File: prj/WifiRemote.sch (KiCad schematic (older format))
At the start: 68 parts, among them J1 DIP-BLACK-MALE-HEADER-VERT_4P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, J2 DIP-BLACK-MALE-HEADER_6P-2.54_, K1 DIP-SWITCH-TACTILE-SPST-NO_TS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, K2 DIP-SWITCH-TACTILE-SPST-NO_TS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, K3 DIP-SWITCH-TACTILE-SPST-NO_TS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, K4 DIP-SWITCH-TACTILE-SPST-NO_TS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, M1 Mechanical_Mount, M2 Mechanical_Mount, M3 Mechanical_Mount, M4 Mechanical_Mount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

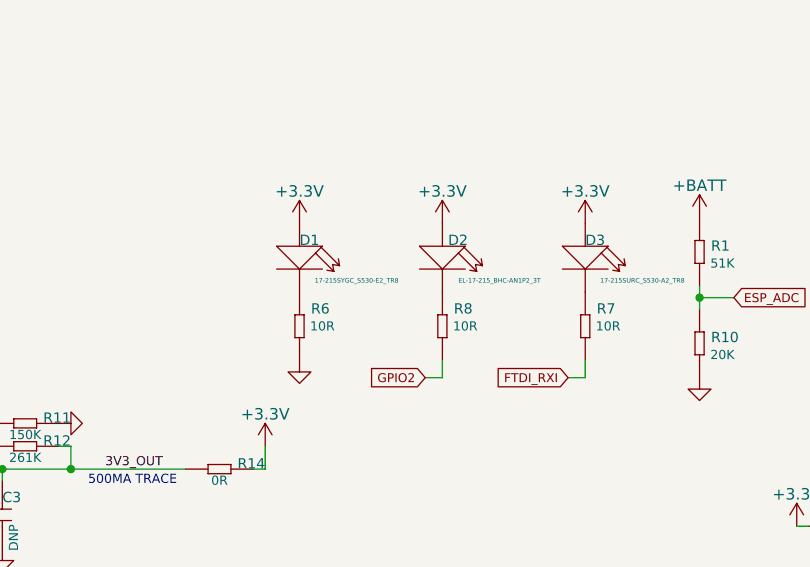
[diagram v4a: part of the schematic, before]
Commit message: Swapped D1 and D2 for layout
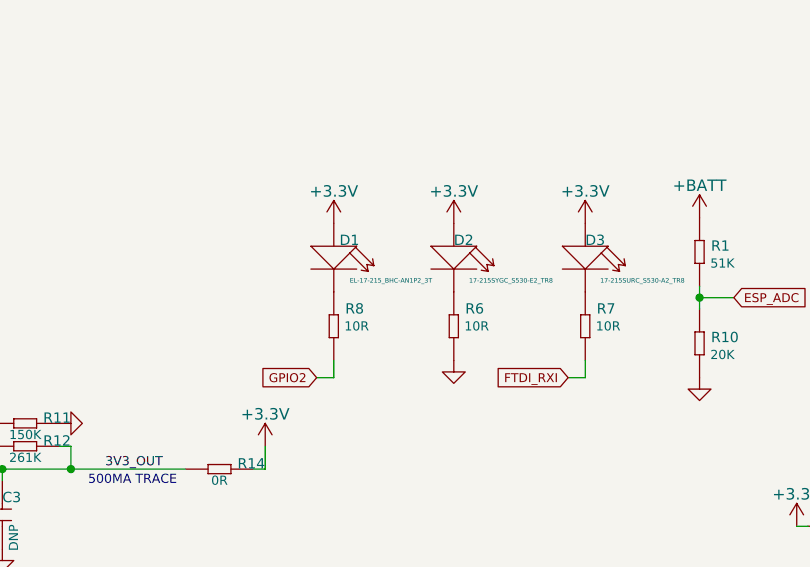
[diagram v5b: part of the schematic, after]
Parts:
- renumbered D2 to D1, D1 to D2
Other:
- moved on the sheet: D1, D2, R6, R8
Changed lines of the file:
@@
 $EndComp
 $Comp
-L SMD-LED-CLEAR-GREEN_0805_ D1
+L SMD-LED-CLEAR-GREEN_0805_ D2
 U 1 1 59B8B400
-P 4800 1225
-F 0 "D1" V 4750 1225 45  0000 L BNN
-F 1 "SMD-LED-CLEAR-GREEN_0805_" H 4600 1025 45  0001 L BNN
-F 2 "SeeedOPL-LED-2016:LED-0805" H 4800 1225 60  0001 C CNN
-F 3 "" H 4800 1225 60  0000 C CNN
-F 4 "17-215SYGC_S530-E2_TR8" V 4900 1475 20  0000 C CNN "MPN"
-F 5 "304090057" H 4830 1375 20  0001 C CNN "SKU"
-	1    4800 1225
+P 5475 1225
+F 0 "D2" V 5425 1225 45  0000 L BNN
+F 1 "SMD-LED-CLEAR-GREEN_0805_" H 5275 1025 45  0001 L BNN
+F 2 "SeeedOPL-LED-2016:LED-0805" H 5475 1225 60  0001 C CNN
+F 3 "" H 5475 1225 60  0000 C CNN
+F 4 "17-215SYGC_S530-E2_TR8" V 5575 1475 20  0000 C CNN "MPN"
+F 5 "304090057" H 5505 1375 20  0001 C CNN "SKU"
+	1    5475 1225
 	0    1    1    0
 $EndComp
@@
 L +3.3V #PWR024
 U 1 1 59B8BA53
-P 4800 1075
-F 0 "#PWR024" H 4800 925 50  0001 C CNN
-F 1 "+3.3V" H 4800 1215 50  0000 C CNN
-F 2 "" H 4800 1075 50  0000 C CNN
-F 3 "" H 4800 1075 50  0000 C CNN
-	1    4800 1075
+P 5475 1075
+F 0 "#PWR024" H 5475 925 50  0001 C CNN
+F 1 "+3.3V" H 5475 1215 50  0000 C CNN
+F 2 "" H 5475 1075 50  0000 C CNN
+F 3 "" H 5475 1075 50  0000 C CNN
+	1    5475 1075
 	1    0    0    -1
 $EndComp
@@
 L SMD-RES-10R-5%-1_10W_0603_ R6
 U 1 1 59B8BFB0
-P 4800 1525
-F 0 "R6" V 4750 1575 45  0000 L BNN
-F 1 "SMD-RES-10R-5%-1_10W_0603_" H 4650 1425 45  0001 L BNN
-F 2 "SeeedOPL-Resistor-2016:R0603" H 4800 1525 40  0001 C CNN
-F 3 "" H 4800 1525 40  0001 C CNN
-F 4 "RC0603JR-0710RL" H 4830 1675 20  0001 C CNN "MPN"
-F 5 "301010096" H 4830 1675 20  0001 C CNN "SKU"
-F 6 "10R" V 4800 1625 40  0000 C CNN "RESISTANCE"
-	1    4800 1525
+P 5475 1525
+F 0 "R6" V 5425 1575 45  0000 L BNN
+F 1 "SMD-RES-10R-5%-1_10W_0603_" H 5325 1425 45  0001 L BNN
+F 2 "SeeedOPL-Resistor-2016:R0603" H 5475 1525 40  0001 C CNN
+F 3 "" H 5475 1525 40  0001 C CNN
+F 4 "RC0603JR-0710RL" H 5505 1675 20  0001 C CNN "MPN"
+F 5 "301010096" H 5505 1675 20  0001 C CNN "SKU"
+F 6 "10R" V 5475 1625 40  0000 C CNN "RESISTANCE"
+	1    5475 1525
 	0    1    1    0
 $EndComp
@@
 L GNDD #PWR025
 U 1 1 59B8C077
-P 4800 1675
-F 0 "#PWR025" H 4800 1425 50  0001 C CNN
-F 1 "GNDD" H 4800 1525 50  0001 C CNN
-F 2 "" H 4800 1675 50  0000 C CNN
-F 3 "" H 4800 1675 50  0000 C CNN
-	1    4800 1675
+P 5475 1675
+F 0 "#PWR025" H 5475 1425 50  0001 C CNN
+F 1 "GNDD" H 5475 1525 50  0001 C CNN
+F 2 "" H 5475 1675 50  0000 C CNN
+F 3 "" H 5475 1675 50  0000 C CNN
+	1    5475 1675
 	1    0    0    -1
 $EndComp
@@
 	0    -1   -1   0
 $EndComp
-Text GLabel 5350 1750 0    39   Input ~ 0
+Text GLabel 4875 1750 0    39   Input ~ 0
 GPIO2
 Text GLabel 8000 1250 0    39   Input ~ 0
@@
 L SMD-RES-10R-5%-1_10W_0603_ R8
 U 1 1 59B9052C
-P 5425 1525
-F 0 "R8" V 5375 1575 45  0000 L BNN
-F 1 "SMD-RES-10R-5%-1_10W_0603_" H 5275 1425 45  0001 L BNN
-F 2 "SeeedOPL-Resistor-2016:R0603" H 5425 1525 40  0001 C CNN
-F 3 "" H 5425 1525 40  0001 C CNN
-F 4 "RC0603JR-0710RL" H 5455 1675 20  0001 C CNN "MPN"
-F 5 "301010096" H 5455 1675 20  0001 C CNN "SKU"
-F 6 "10R" V 5425 1625 40  0000 C CNN "RESISTANCE"
-	1    5425 1525
+P 4950 1525
+F 0 "R8" V 4900 1575 45  0000 L BNN
+F 1 "SMD-RES-10R-5%-1_10W_0603_" H 4800 1425 45  0001 L BNN
+F 2 "SeeedOPL-Resistor-2016:R0603" H 4950 1525 40  0001 C CNN
+F 3 "" H 4950 1525 40  0001 C CNN
+F 4 "RC0603JR-0710RL" H 4980 1675 20  0001 C CNN "MPN"
+F 5 "301010096" H 4980 1675 20  0001 C CNN "SKU"
+F 6 "10R" V 4950 1625 40  0000 C CNN "RESISTANCE"
+	1    4950 1525
 	0    1    1    0
 $EndComp
@@
 L +3.3V #PWR030
 U 1 1 59B94182
-P 5425 1075
-F 0 "#PWR030" H 5425 925 50  0001 C CNN
-F 1 "+3.3V" H 5425 1215 50  0000 C CNN
-F 2 "" H 5425 1075 50  0000 C CNN
-F 3 "" H 5425 1075 50  0000 C CNN
-	1    5425 1075
+P 4950 1075
+F 0 "#PWR030" H 4950 925 50  0001 C CNN
+F 1 "+3.3V" H 4950 1215 50  0000 C CNN
+F 2 "" H 4950 1075 50  0000 C CNN
+F 3 "" H 4950 1075 50  0000 C CNN
+	1    4950 1075
 	1    0    0    -1
 $EndComp
@@
 	7850 2425 7850 2400
 Wire Wire Line
-	5350 1750 5425 1750
-Wire Wire Line
-	5425 1750 5425 1675
+	4875 1750 4950 1750
+Wire Wire Line
+	4950 1750 4950 1675
 Wire Wire Line
 	5975 1750 6050 1750
@@
 MOUNTING HARDWARE
 $Comp
-L SMD-LED-CLEAR-BLUE_0805_ D2
+L SMD-LED-CLEAR-BLUE_0805_ D1
 U 1 1 59C1E2BF
-P 5425 1225
-F 0 "D2" V 5375 1250 45  0000 L BNN
-F 1 "SMD-LED-CLEAR-BLUE_0805_" H 5225 1025 45  0001 L BNN
-F 2 "SeeedOPL-LED-2016:LED-0805" H 5425 1225 60  0001 C CNN
-F 3 "" H 5425 1225 60  0001 C CNN
-F 4 "EL-17-215_BHC-AN1P2_3T" V 5525 1475 20  0000 C CNN "MPN"
-F 5 "304090061" H 5455 1375 20  0001 C CNN "SKU"
-	1    5425 1225
-	0    1    1    0
-$EndComp
+P 4950 1225
+F 0 "D1" V 4900 1250 45  0000 L BNN
+F 1 "SMD-LED-CLEAR-BLUE_0805_" H 4750 1025 45  0001 L BNN
+F 2 "SeeedOPL-LED-2016:LED-0805" H 4950 1225 60  0001 C CNN
+F 3 "" H 4950 1225 60  0001 C CNN
+F 4 "EL-17-215_BHC-AN1P2_3T" V 5050 1475 20  0000 C CNN "MPN"
+F 5 "304090061" H 4980 1375 20  0001 C CNN "SKU"
+	1    4950 1225
+	0    1    1    0
+$EndComp

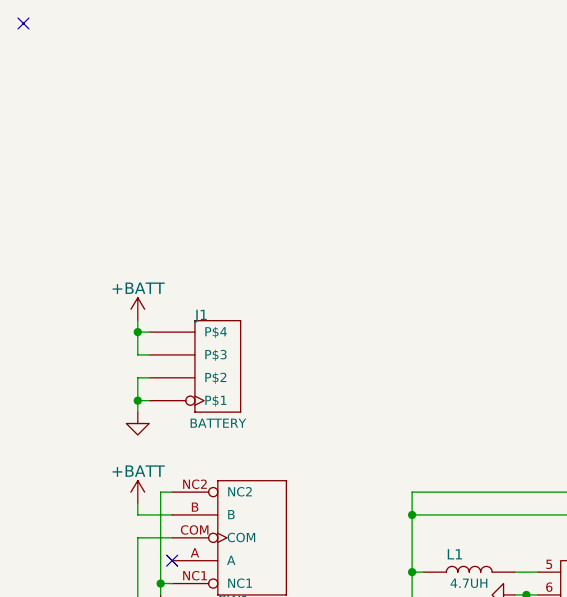
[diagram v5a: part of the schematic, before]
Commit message: Updated battery connector
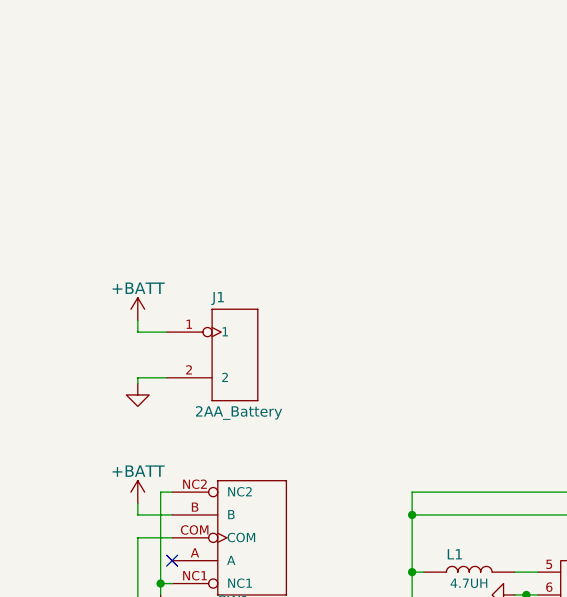
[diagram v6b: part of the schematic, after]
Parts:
- removed J1: DIP-BLACK-MALE-HEADER-VERT_4P-2.54_, SeeedOPL-Connector-2016:H4-2.54, symbol DIP-BLACK-MALE-HEADER-VERT_4P-2.54_
- added J1: 2AA_Battery, SeeedOPL-Connector-2016:H2-2.54, symbol 2AA_Battery
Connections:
- net +BATT: now also J1.1
- net GNDD: now also J1.2
- no-connect marks 11 -> 10
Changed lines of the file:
@@
 LIBS:ICEE-Diode
 LIBS:ICEE-Mechanical
+LIBS:ICEE-Battery
 EELAYER 25 0
 EELAYER END
@@
 	1    0    0    -1
 $EndComp
-NoConn ~ 250  -550
-$Comp
-L DIP-BLACK-MALE-HEADER-VERT_4P-2.54_ J1
-U 1 1 59B7E14C
-P 1100 950
-F 0 "J1" H 1000 700 45  0000 L BNN
-F 1 "DIP-BLACK-MALE-HEADER-VERT_4P-2.54_" H 1050 1200 45  0001 L BNN
-F 2 "SeeedOPL-Connector-2016:H4-2.54" H 1100 950 60  0001 C CNN
-F 3 "" H 1100 950 60  0001 C CNN
-F 4 "P125-1104A0BS116A1" H 1130 1100 20  0001 C CNN "MPN"
-F 5 "320020017" H 1130 1100 20  0001 C CNN "SKU"
-F 6 "BATTERY" H 1100 1200 40  0000 C CNN "DESCRIPTION"
-	1    1100 950
-	1    0    0    1
-$EndComp
 $Comp
 L GNDD #PWR023
 U 1 1 59B82986
-P 750 1150
-F 0 "#PWR023" H 750 900 50  0001 C CNN
-F 1 "GNDD" H 750 1000 50  0001 C CNN
-F 2 "" H 750 1150 50  0000 C CNN
-F 3 "" H 750 1150 50  0000 C CNN
-	1    750  1150
+P 750 1025
+F 0 "#PWR023" H 750 775 50  0001 C CNN
+F 1 "GNDD" H 750 875 50  0001 C CNN
+F 2 "" H 750 1025 50  0000 C CNN
+F 3 "" H 750 1025 50  0000 C CNN
+	1    750  1025
 	1    0    0    -1
 $EndComp
@@
 Connection ~ 4275 5625
 Wire Wire Line
-	800  800  750  800
-Wire Wire Line
-	750  750  750  900
-Wire Wire Line
-	750  900  800  900
-Connection ~ 750  800
-Wire Wire Line
-	800  1000 750  1000
-Wire Wire Line
-	750  1000 750  1150
-Wire Wire Line
-	750  1100 800  1100
-Connection ~ 750  1100
-Wire Wire Line
 	6975 2400 7025 2400
 Wire Wire Line
@@
 	1    0    0    -1
 $EndComp
+$Comp
+L 2AA_Battery J1
+U 1 1 59C7F15C
+P 1175 900
+F 0 "J1" H 1075 1125 45  0000 L BNN
+F 1 "2AA_Battery" H 1000 625 45  0000 L BNN
+F 2 "SeeedOPL-Connector-2016:H2-2.54" H 1175 900 60  0001 C CNN
+F 3 "" H 1175 900 60  0001 C CNN
+F 4 "BH-321-1A" H 1205 1050 20  0001 C CNN "MPN"
+F 5 "320180001" H 1205 1050 20  0001 C CNN "SKU"
+	1    1175 900
+	1    0    0    -1
+$EndComp
+Wire Wire Line
+	875  800  750  800
+Wire Wire Line
+	750  800  750  750
+Wire Wire Line
+	875  1000 750  1000
+Wire Wire Line
+	750  1000 750  1025
 $EndSCHEMATC

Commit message: Added footprint for header_1x2
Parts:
- J1: footprint SeeedOPL-Connector-2016:H2-2.54 -> ICEE-Connector:header_1x2
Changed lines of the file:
@@
-	1    0    0    -1
-$EndComp
-$Comp
-L 2AA_Battery J1
-U 1 1 59C7F15C
-P 1175 900
-F 0 "J1" H 1075 1125 45  0000 L BNN
-F 1 "2AA_Battery" H 1000 625 45  0000 L BNN
-F 2 "SeeedOPL-Connector-2016:H2-2.54" H 1175 900 60  0001 C CNN
-F 3 "" H 1175 900 60  0001 C CNN
-F 4 "BH-321-1A" H 1205 1050 20  0001 C CNN "MPN"
-F 5 "320180001" H 1205 1050 20  0001 C CNN "SKU"
-	1    1175 900
 	1    0    0    -1
 $EndComp
@@
 Wire Wire Line
 	750  1000 750  1025
+$Comp
+L 2AA_Battery J1
+U 1 1 59C7F5DA
+P 1175 900
+F 0 "J1" H 1075 1125 45  0000 L BNN
+F 1 "2AA_Battery" H 1000 625 45  0000 L BNN
+F 2 "ICEE-Connector:header_1x2" H 1175 900 60  0001 C CNN
+F 3 "" H 1175 900 60  0001 C CNN
+F 4 "BH-321-1A" H 1205 1050 20  0001 C CNN "MPN"
+F 5 "320180001" H 1205 1050 20  0001 C CNN "SKU"
+	1    1175 900
+	1    0    0    -1
+$EndComp
 $EndSCHEMATC

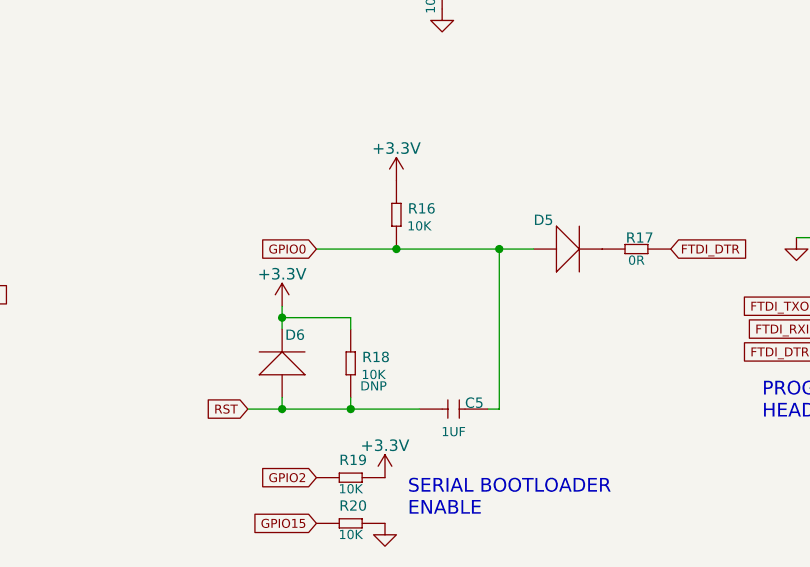
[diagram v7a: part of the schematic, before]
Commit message: Swapped diode packages
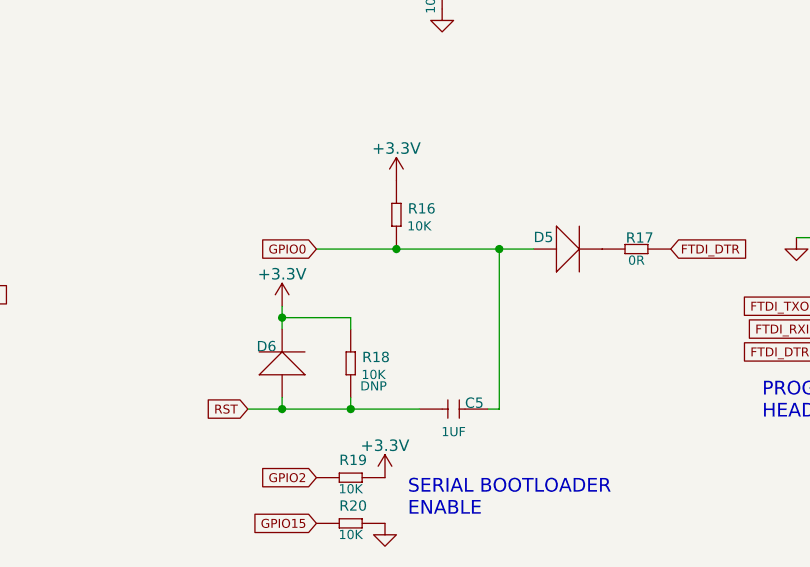
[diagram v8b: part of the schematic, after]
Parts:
- removed D11, D7, D8, D9: SMD-DIODE-SWITCH-1N4148_LL-34_, SeeedOPL-Diode-2016:LL-34, symbol SMD-DIODE-SWITCH-1N4148_LL-34_
- removed D5, D6: SMD-DIODE-SCHOTTKY-20V-500MA_SOD-123_, SeeedOPL-Diode-2016:SOD-123, symbol SMD-DIODE-SCHOTTKY-20V-500MA_SOD-123_
- added D11, D5, D6, D7, D8, D9: SMD-DIODE-SCHOTTKY-20V-1A_SOD-123_, symbol SMD-DIODE-SCHOTTKY-20V-1A_SOD-123_
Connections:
- net +3V3: now also D6.-
- net GPIO0: now also D5.+
- net GPIO13: now also D11.+, D7.+, D8.+, D9.+
- net RST: now also D6.+
- net SW1: now also D7.-
- net SW2: now also D8.-
- net SW3: now also D9.-
- net SW4: now also D11.-
- net at R17.2: now also D5.-
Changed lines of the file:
@@
 GPIO14
-$Comp
-L SMD-DIODE-SWITCH-1N4148_LL-34_ D9
-U 1 1 59AF0C4B
-P 4825 4475
-F 0 "D9" H 4675 4575 45  0000 L BNN
-F 1 "SMD-DIODE-SWITCH-1N4148_LL-34_" H 4675 4325 45  0001 L BNN
-F 2 "SeeedOPL-Diode-2016:LL-34" H 4825 4475 60  0001 C CNN
-F 3 "" H 4825 4475 60  0001 C CNN
-F 4 "1N4148" H 4855 4625 20  0001 C CNN "MPN"
-F 5 "304040016" H 4855 4625 20  0001 C CNN "SKU"
-	1    4825 4475
-	-1   0    0    1
-$EndComp
-$Comp
-L SMD-DIODE-SWITCH-1N4148_LL-34_ D11
-U 1 1 59AF1CC4
-P 4825 4725
-F 0 "D11" H 4675 4825 45  0000 L BNN
-F 1 "SMD-DIODE-SWITCH-1N4148_LL-34_" H 4675 4575 45  0001 L BNN
-F 2 "SeeedOPL-Diode-2016:LL-34" H 4825 4725 60  0001 C CNN
-F 3 "" H 4825 4725 60  0001 C CNN
-F 4 "1N4148" H 4855 4875 20  0001 C CNN "MPN"
-F 5 "304040016" H 4855 4875 20  0001 C CNN "SKU"
-	1    4825 4725
-	-1   0    0    1
-$EndComp
-$Comp
-L SMD-DIODE-SWITCH-1N4148_LL-34_ D8
-U 1 1 59AF1E3D
-P 4825 4225
-F 0 "D8" H 4675 4325 45  0000 L BNN
-F 1 "SMD-DIODE-SWITCH-1N4148_LL-34_" H 4675 4075 45  0001 L BNN
-F 2 "SeeedOPL-Diode-2016:LL-34" H 4825 4225 60  0001 C CNN
-F 3 "" H 4825 4225 60  0001 C CNN
-F 4 "1N4148" H 4855 4375 20  0001 C CNN "MPN"
-F 5 "304040016" H 4855 4375 20  0001 C CNN "SKU"
-	1    4825 4225
-	-1   0    0    1
-$EndComp
-$Comp
-L SMD-DIODE-SWITCH-1N4148_LL-34_ D7
-U 1 1 59AF1EFF
-P 4825 3975
-F 0 "D7" H 4675 4075 45  0000 L BNN
-F 1 "SMD-DIODE-SWITCH-1N4148_LL-34_" H 4675 3825 45  0001 L BNN
-F 2 "SeeedOPL-Diode-2016:LL-34" H 4825 3975 60  0001 C CNN
-F 3 "" H 4825 3975 60  0001 C CNN
-F 4 "1N4148" H 4855 4125 20  0001 C CNN "MPN"
-F 5 "304040016" H 4855 4125 20  0001 C CNN "SKU"
-	1    4825 3975
-	-1   0    0    1
-$EndComp
 $Comp
 L SMD-RES-10K-5%-1_10W_0603_ R26
@@
 	1    5225 3775
 	0    1    1    0
-$EndComp
-$Comp
-L SMD-DIODE-SCHOTTKY-20V-500MA_SOD-123_ D5
-U 1 1 59AFC988
-P 8400 3775
-F 0 "D5" H 8250 3875 45  0000 L BNN
-F 1 "SMD-DIODE-SCHOTTKY-20V-500MA_SOD-123_" H 8250 3625 45  0001 L BNN
-F 2 "SeeedOPL-Diode-2016:SOD-123" H 8400 3775 60  0001 C CNN
-F 3 "" H 8400 3775 60  0001 C CNN
-F 4 "SS0520-7-F" H 8430 3925 20  0001 C CNN "MPN"
-F 5 "304020032" H 8430 3925 20  0001 C CNN "SKU"
-	1    8400 3775
-	1    0    0    -1
 $EndComp
 $Comp
@@
 	1    0    0    -1
 $EndComp
-$Comp
-L SMD-DIODE-SCHOTTKY-20V-500MA_SOD-123_ D6
-U 1 1 59B9AAAC
-P 7150 4275
-F 0 "D6" V 7300 4175 45  0000 L BNN
-F 1 "SMD-DIODE-SCHOTTKY-20V-500MA_SOD-123_" H 7000 4125 45  0001 L BNN
-F 2 "SeeedOPL-Diode-2016:SOD-123" H 7150 4275 60  0001 C CNN
-F 3 "" H 7150 4275 60  0001 C CNN
-F 4 "SS0520-7-F" H 7180 4425 20  0001 C CNN "MPN"
-F 5 "304020032" H 7180 4425 20  0001 C CNN "SKU"
-	1    7150 4275
-	0    -1   -1   0
-$EndComp
 Text GLabel 4875 1750 0    39   Input ~ 0
 GPIO2
@@
 	1    0    0    -1
 $EndComp
+$Comp
+L SMD-DIODE-SCHOTTKY-20V-1A_SOD-123_ D7
+U 1 1 59C8DC29
+P 4825 3975
+F 0 "D7" H 4675 4075 45  0000 L BNN
+F 1 "SMD-DIODE-SCHOTTKY-20V-1A_SOD-123_" H 4675 3825 45  0001 L BNN
+F 2 "" H 4825 3975 60  0001 C CNN
+F 3 "" H 4825 3975 60  0001 C CNN
+F 4 "B5819W" H 4855 4125 20  0001 C CNN "MPN"
+F 5 "304020034" H 4855 4125 20  0001 C CNN "SKU"
+	1    4825 3975
+	-1   0    0    1
+$EndComp
+$Comp
+L SMD-DIODE-SCHOTTKY-20V-1A_SOD-123_ D8
+U 1 1 59C8E639
+P 4825 4225
+F 0 "D8" H 4675 4325 45  0000 L BNN
+F 1 "SMD-DIODE-SCHOTTKY-20V-1A_SOD-123_" H 4675 4075 45  0001 L BNN
+F 2 "" H 4825 4225 60  0001 C CNN
+F 3 "" H 4825 4225 60  0001 C CNN
+F 4 "B5819W" H 4855 4375 20  0001 C CNN "MPN"
+F 5 "304020034" H 4855 4375 20  0001 C CNN "SKU"
+	1    4825 4225
+	-1   0    0    1
+$EndComp
+$Comp
+L SMD-DIODE-SCHOTTKY-20V-1A_SOD-123_ D9
+U 1 1 59C8E959
+P 4825 4475
+F 0 "D9" H 4675 4575 45  0000 L BNN
+F 1 "SMD-DIODE-SCHOTTKY-20V-1A_SOD-123_" H 4675 4325 45  0001 L BNN
+F 2 "" H 4825 4475 60  0001 C CNN
+F 3 "" H 4825 4475 60  0001 C CNN
+F 4 "B5819W" H 4855 4625 20  0001 C CNN "MPN"
+F 5 "304020034" H 4855 4625 20  0001 C CNN "SKU"
+	1    4825 4475
+	-1   0    0    1
+$EndComp
+$Comp
+L SMD-DIODE-SCHOTTKY-20V-1A_SOD-123_ D11
+U 1 1 59C8ECBC
+P 4825 4725
+F 0 "D11" H 4675 4825 45  0000 L BNN
+F 1 "SMD-DIODE-SCHOTTKY-20V-1A_SOD-123_" H 4675 4575 45  0001 L BNN
+F 2 "" H 4825 4725 60  0001 C CNN
+F 3 "" H 4825 4725 60  0001 C CNN
+F 4 "B5819W" H 4855 4875 20  0001 C CNN "MPN"
+F 5 "304020034" H 4855 4875 20  0001 C CNN "SKU"
+	1    4825 4725
+	-1   0    0    1
+$EndComp
+$Comp
+L SMD-DIODE-SCHOTTKY-20V-1A_SOD-123_ D6
+U 1 1 59C8EFD1
+P 7150 4275
+F 0 "D6" V 7250 4300 45  0000 L BNN
+F 1 "SMD-DIODE-SCHOTTKY-20V-1A_SOD-123_" H 7000 4125 45  0001 L BNN
+F 2 "" H 7150 4275 60  0001 C CNN
+F 3 "" H 7150 4275 60  0001 C CNN
+F 4 "B5819W" H 7180 4425 20  0001 C CNN "MPN"
+F 5 "304020034" H 7180 4425 20  0001 C CNN "SKU"
+	1    7150 4275
+	0    -1   -1   0
+$EndComp
+$Comp
+L SMD-DIODE-SCHOTTKY-20V-1A_SOD-123_ D5
+U 1 1 59C90176
+P 8400 3775
+F 0 "D5" H 8250 3800 45  0000 L BNN
+F 1 "SMD-DIODE-SCHOTTKY-20V-1A_SOD-123_" H 8250 3625 45  0001 L BNN
+F 2 "" H 8400 3775 60  0001 C CNN
+F 3 "" H 8400 3775 60  0001 C CNN
+F 4 "B5819W" H 8430 3925 20  0001 C CNN "MPN"
+F 5 "304020034" H 8430 3925 20  0001 C CNN "SKU"
+	1    8400 3775
+	1    0    0    -1
+$EndComp
